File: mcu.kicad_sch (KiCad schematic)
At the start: 32 parts, among them SW2 SW_SPDT, U2 STM32F429ZITx, Y3 Crystal_GND24

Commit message: More MCU wiring
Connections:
- net USB_OTG_FS_ID is gone; now on net UART0_RX: U2.102 (PA10)
- net SPI0_DO: now also U2.43 (PA7); no longer U2.135 (PB5)
- net UART0_RX: no longer U2.137 (PB7)
- net UART1_RX: now also U2.37 (PA3); no longer U2.122 (PD6)
- net UART1_TX: now also U2.36 (PA2); no longer U2.119 (PD5)
- net JTAG0_TDI: now reaches U2.110 (PA15)
- net JTAG0_TDO: now reaches U2.133 (PB3)
- net SPI1_DI: no longer names the net of U2.75 (PB14)
- net SPI1_DO: no longer names the net of U2.76 (PB15)
- net SPI1_SK: no longer names the net of U2.69 (PB10)
- net SWCLK renamed JTAG0_TCK
- net SWDIO renamed JTAG0_TMS
- new net I2C0_SDA: U2.137 (PB7)
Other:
- note added: "1: Boot Flash 3: Boot System Memory (STM Bootloader)"

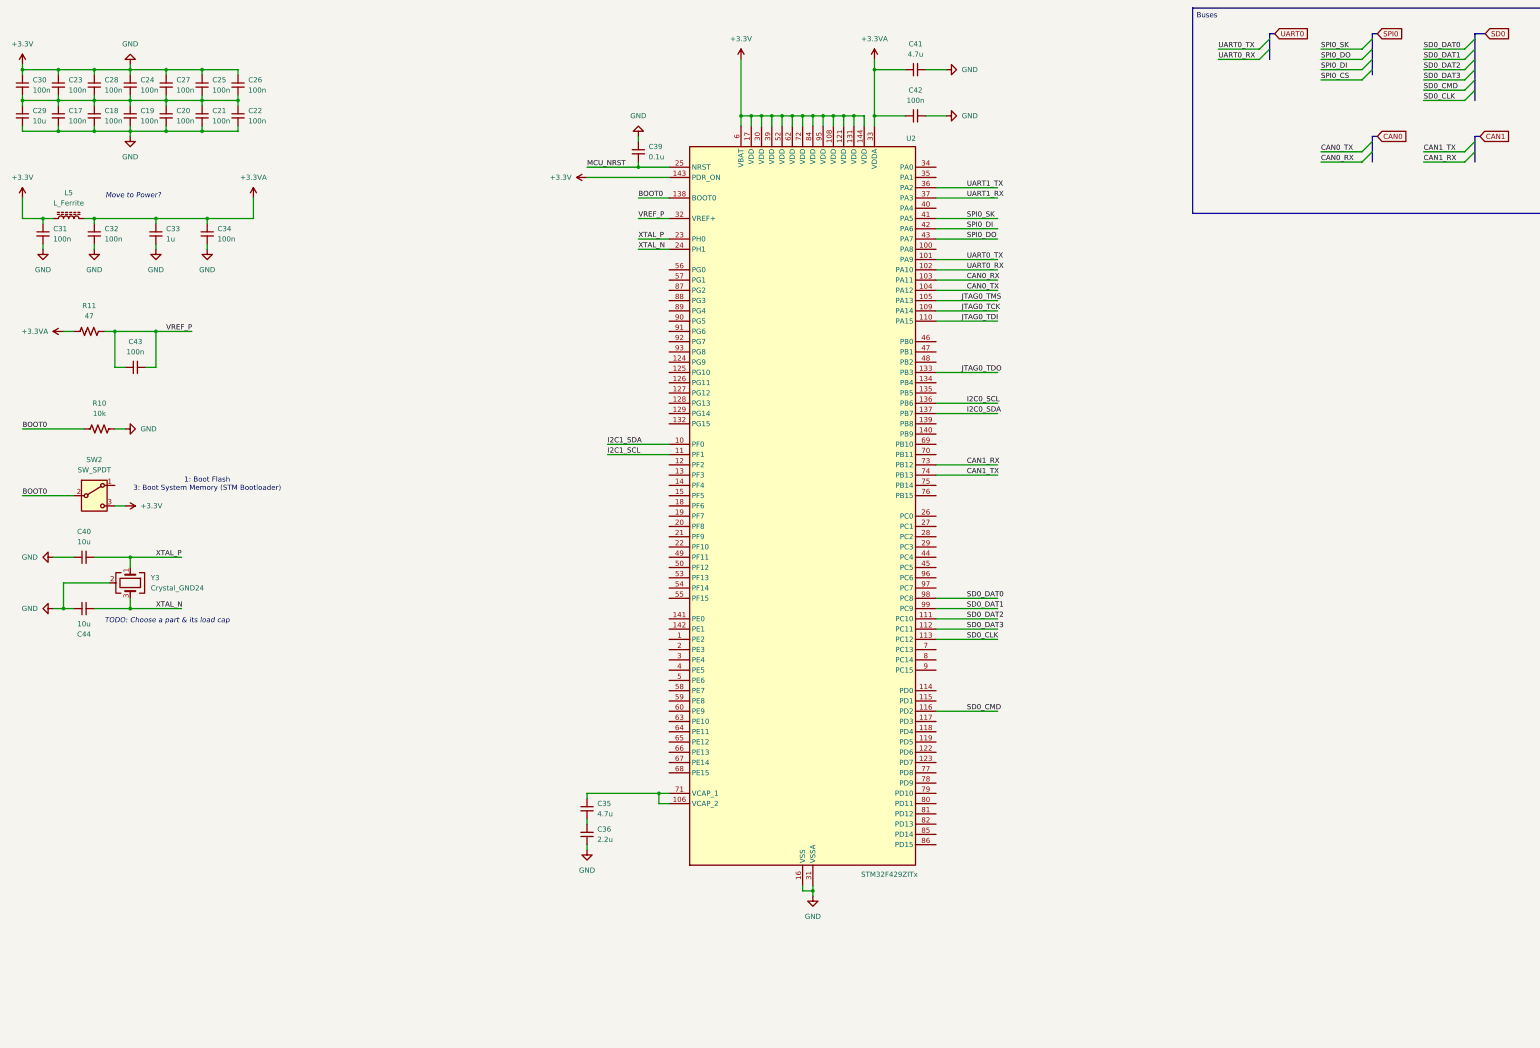
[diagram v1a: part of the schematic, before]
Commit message: A lot re-wiring, added appropriate parts for schematic components. Some re-organization.
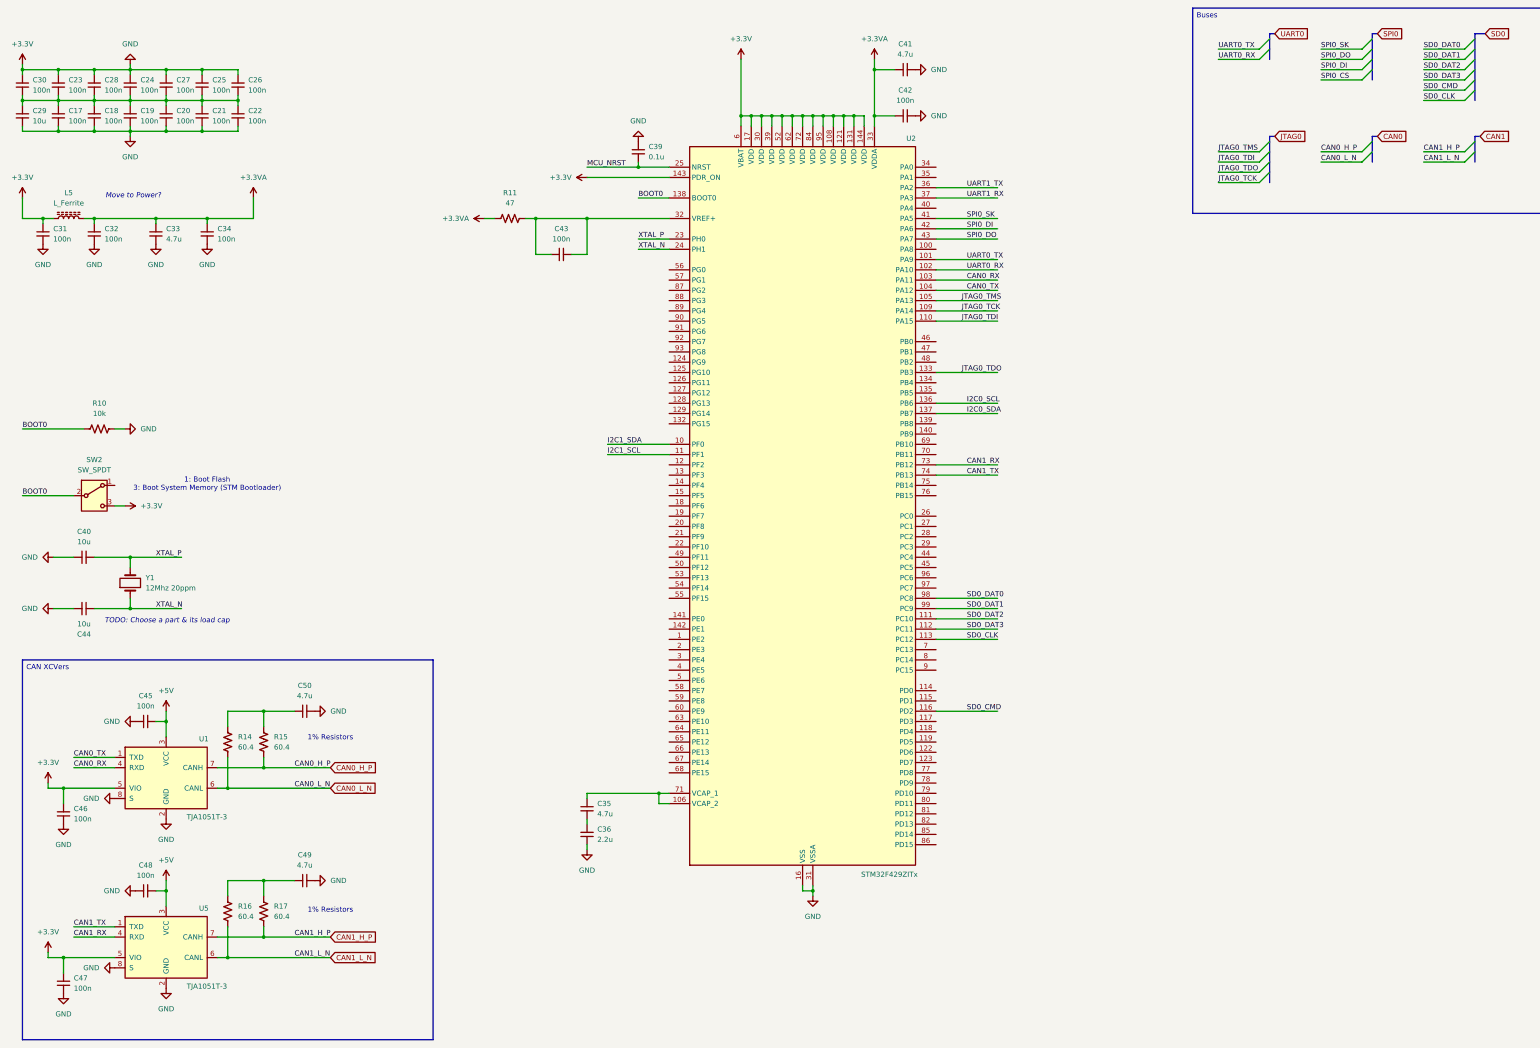
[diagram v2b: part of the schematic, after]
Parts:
- removed Y3: Crystal_GND24, symbol Device:Crystal_GND24
- added C45, C46, C47, C48: 100n, symbol Device:C_Small
- added C49, C50: 4.7u, symbol Device:C_Small
- added R14, R15, R16, R17: 60.4, symbol Device:R_US
- added U1, U5: TJA1051T-3, Package_SO:SOIC-8_3.9x4.9mm_P1.27mm, symbol Interface_CAN_LIN:TJA1051T-3
- added Y1: 12Mhz 20ppm, symbol Device:Crystal
- C33: value 1u -> 4.7u
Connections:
- net +3.3V: now also C45.1, C46.1, C46.2, C47.1, C47.2, C48.1, C49.2, C50.2, U1.2 (GND), U1.5 (VIO), U1.8 (S), U5.2 (GND), U5.5 (VIO), U5.8 (S)
- net CAN0_RX: now also U1.4 (RXD)
- net CAN0_TX: now also U1.1 (TXD)
- net CAN1_RX: now also U5.4 (RXD)
- net CAN1_TX: now also U5.1 (TXD)
- net XTAL_N: now also Y1.1
- net XTAL_P: now also Y1.2
- net VREF_P: no longer names the net of C43.1, C43.2, R11.2, U2.32 (VREF+)
- new net: C49.1, R16.1, R17.1
- new net: C50.1, R14.1, R15.1
- new net +5V: C45.2, C48.2, U1.3 (VCC), U5.3 (VCC)
- new net CAN0_H_P: R15.2, U1.7 (CANH)
- new net CAN0_L_N: R14.2, U1.6 (CANL)
- new net CAN1_H_P: R17.2, U5.7 (CANH)
- new net CAN1_L_N: R16.2, U5.6 (CANL)
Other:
- note added: "1% Resistors"
- moved on the sheet: C41, C42, C43, R11

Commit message: Alot of stuff
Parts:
- removed SW2: SW_SPDT, symbol Switch:SW_SPDT
- added D10: RED_LED1, LED_SMD:LED_0805_2012Metric, symbol Device:LED
- added D6: MCU_GOOD_LED, LED_SMD:LED_0805_2012Metric, symbol Device:LED
- added D7: GREEN_LED1, LED_SMD:LED_0805_2012Metric, symbol Device:LED
- added D9: BLUE_LED1, LED_SMD:LED_0805_2012Metric, symbol Device:LED
- added R20, R22, R23: 3.3k, symbol Device:R_US
- added R25, R26, R28, R29: 560, symbol Device:R_US
- R10: value 10k -> 3.3k
- Y1: footprint (none) -> SamacSys_Parts:ABLS7
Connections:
- net I2C0_SCL is gone; now on net I2C1_SCL: U2.136 (PB6)
- net I2C0_SDA is gone; now on net I2C1_SDA: U2.137 (PB7)
- net UART0_RX is gone; now on net UART1_RX: U2.102 (PA10)
- net UART0_TX is gone; now on net UART1_TX: U2.101 (PA9)
- net +3.3V: now also D10.1 (K), D6.1 (K), D7.1 (K), D9.1 (K), R20.2, R22.2, R23.2
- net CAN0_RX: no longer U2.103 (PA11)
- net CAN0_TX: no longer U2.104 (PA12)
- net CAN1_RX: now also U2.103 (PA11); no longer U2.73 (PB12)
- net CAN1_TX: now also U2.104 (PA12); no longer U2.74 (PB13)
- net I2C1_SCL: now also R20.1; no longer U2.11 (PF1)
- net I2C1_SDA: now also R10.1; no longer U2.10 (PF0)
- net UART1_RX: no longer U2.37 (PA3)
- net UART1_TX: no longer U2.36 (PA2)
- net GPIO8: now reaches U2.124 (PG9)
- net GPIO9: now reaches U2.125 (PG10)
- net GPIO10: now reaches U2.126 (PG11)
- net GPIO11: now reaches U2.127 (PG12)
- net GPIO12: now reaches U2.128 (PG13)
- net GPIO13: now reaches U2.129 (PG14)
- net GPIO14: now reaches U2.132 (PG15)
- net GREEN_LED1: now reaches U2.141 (PE0)
- net GREEN_LED1: now also R26.2
- net BLUE_LED1: now reaches U2.142 (PE1)
- net BLUE_LED1: now also R28.2
- net MCU_BOOT1: now reaches U2.48 (PB2)
- net MCU_GOOD_LED: now reaches U2.56 (PG0)
- net MCU_GOOD_LED: now also R25.2
- net GPIO0: now reaches U2.57 (PG1)
- net RED_LED1: now reaches U2.66 (PE13)
- net RED_LED1: now also R29.2
- net GPIO1: now reaches U2.87 (PG2)
- net GPIO2: now reaches U2.88 (PG3)
- net GPIO3: now reaches U2.89 (PG4)
- net GPIO4: now reaches U2.90 (PG5)
- net GPIO5: now reaches U2.91 (PG6)
- net GPIO6: now reaches U2.92 (PG7)
- net GPIO7: now reaches U2.93 (PG8)
- net BOOT0 renamed MCU_BOOT0
- net MCU_BOOT0: no longer R10.1
- net JTAG0_TCK renamed JTAG_TCK
- net JTAG0_TDI renamed JTAG_TDI
- net JTAG0_TDO renamed JTAG_TDO
- net JTAG0_TMS renamed JTAG_TMS
- net SD0_CLK renamed SD_CLK
- net SD0_CMD renamed SD_CMD
- net SD0_DAT0 renamed SD_DAT0
- net SD0_DAT1 renamed SD_DAT1
- net SD0_DAT2 renamed SD_DAT2
- net SD0_DAT3 renamed SD_DAT3
- net SPI0_DI renamed SPI1_DI
- net SPI0_DO renamed SPI1_DO
- net SPI0_SK renamed SPI1_SK
- new net: D10.2 (A), R29.1
- new net: D6.2 (A), R25.1
- new net: D9.2 (A), R28.1
- new net: D7.2 (A), R26.1
- new net CAN2_RX: U2.73 (PB12)
- new net CAN2_TX: U2.74 (PB13)
- new net I2C2_SCL: R22.1, U2.11 (PF1)
- new net I2C2_SDA: R23.1, U2.10 (PF0)
- new net UART2_RX: U2.37 (PA3)
- new net UART2_TX: U2.36 (PA2)
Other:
- note added: "Use LTST-C170TBKT for all LEDs!"
- note added: "VDDA flitering for ADCs"
- note added: "values for these matter! need fast rise and fall!"
- note removed: "1: Boot Flash 3: Boot System Memory (STM Bootloader)"
- note removed: "Move to Power?"

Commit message: Stuff
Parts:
- C40, C44: value 10u -> 27p
- Y1: value 12Mhz 20ppm -> 12Mhz; footprint SamacSys_Parts:ABLS7 -> SamacSys_Parts:ABLS7M212000MHZD2YT
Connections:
- net SD_DET: now also U2.7 (PC13)
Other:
- note added: "3.3k good value for I2C open-drain"
- note added: "Need 1% Resistors here!"
- note removed: "1% Resistors"
- note removed: "TODO: Choose a part & its load cap"
- note removed: "values for these matter! need fast rise and fall!"
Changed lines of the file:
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@@
 		)
 	)
-	(text "1% Resistors"
+	(text "Need 1% Resistors here!"
 		(exclude_from_sim no)
-		(at 101.6 239.776 0)
+		(at 104.902 239.776 0)
 		(effects
 			(font
@@
 		)
 	)
-	(text "values for these matter! need fast rise and fall!\n"
+	(text "3.3k good value for I2C open-drain"
 		(exclude_from_sim no)
 		(at 160.528 121.666 0)
@@
 		)
 	)
-	(text "values for these matter! need fast rise and fall!\n"
+	(text "3.3k good value for I2C open-drain"
 		(exclude_from_sim no)
 		(at 277.622 110.49 0)
@@
 		)
 	)
-	(text "TODO: Choose a part & its load cap"
+	(text "Need 1% Resistors here!"
 		(exclude_from_sim no)
-		(at 61.214 168.148 0)
-		(effects
-			(font
-				(size 1.27 1.27)
-				(italic yes)
-			)
-		)
-	)
-	(text "1% Resistors"
-		(exclude_from_sim no)
-		(at 101.6 197.104 0)
+		(at 104.902 197.612 0)
 		(effects
 			(font
@@
 	(wire
 		(pts
+			(xy 251.46 175.26) (xy 266.7 175.26)
+		)
+		(stroke
+			(width 0)
+			(type default)
+		)
+	)
+	(wire
+		(pts
 			(xy 223.52 43.18) (xy 223.52 45.72)
 		)
@@
 		)
 	)
+	(label "SD_DET"
+		(at 266.7 175.26 180)
+		(effects
+			(font
+				(size 1.27 1.27)
+			)
+			(justify right bottom)
+		)
+	)
 	(label "GPIO14"
 		(at 374.65 119.38 0)
@@
 			)
 		)
-		(property "Value" "12Mhz 20ppm"
+		(property "Value" "12Mhz"
 			(at 55.88 160.02 90)
 			(show_name no)
@@
 			)
 		)
-		(property "Footprint" "SamacSys_Parts:ABLS7"
+		(property "Footprint" "SamacSys_Parts:ABLS7M212000MHZD2YT"
 			(at 52.07 158.75 0)
 			(hide yes)
@@
 			)
 		)
-		(property "Description" "Two pin crystal"
+		(property "Description" "ABLS7M212000MHZD2YT Two pin crystal 12Mhz 20ppm"
 			(at 52.07 158.75 0)
 			(hide yes)
@@
 			)
 		)
-		(property "Value" "10u"
+		(property "Value" "27p"
 			(at 40.6337 168.91 90)
 			(show_name no)
@@
 			)
 		)
-		(property "Value" "10u"
+		(property "Value" "27p"
 			(at 40.6463 148.59 90)
 			(show_name no)

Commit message: Minor
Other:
- note added: "use nmost for these?"
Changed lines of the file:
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@@
+		)
+	)
+	(text "use nmost for these?"
+		(exclude_from_sim no)
+		(at 370.586 145.288 0)
+		(effects
+			(font
+				(size 1.27 1.27)
+			)
 		)
 	)

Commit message: Stuff
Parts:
- removed D10: RED_LED1, LED_SMD:LED_0805_2012Metric, symbol Device:LED
- added D8: LED3, SamacSys_Parts:LEDC2012X110N, symbol Device:LED
- D6: value MCU_GOOD_LED -> LED1; footprint LED_SMD:LED_0805_2012Metric -> SamacSys_Parts:LEDC2012X110N
- D7: value GREEN_LED1 -> LED2; footprint LED_SMD:LED_0805_2012Metric -> SamacSys_Parts:LEDC2012X110N
- D9: value BLUE_LED1 -> LED4; footprint LED_SMD:LED_0805_2012Metric -> SamacSys_Parts:LEDC2012X110N
- R25, R26, R28, R29: value 560 -> 62
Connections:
- net +3.3V: now also D8.1 (K)
- net GPIO0: now also U2.56 (PG0); no longer U2.57 (PG1)
- net GPIO1: now also U2.57 (PG1); no longer U2.87 (PG2)
- net GPIO10: now also U2.125 (PG10); no longer U2.126 (PG11)
- net GPIO11: now also U2.126 (PG11); no longer U2.127 (PG12)
- net GPIO12: now also U2.127 (PG12); no longer U2.128 (PG13)
- net GPIO13: now also U2.128 (PG13); no longer U2.129 (PG14)
- net GPIO14: now also U2.129 (PG14); no longer U2.132 (PG15)
- net GPIO2: now also U2.87 (PG2); no longer U2.88 (PG3)
- net GPIO3: now also U2.88 (PG3); no longer U2.89 (PG4)
- net GPIO4: now also U2.89 (PG4); no longer U2.90 (PG5)
- net GPIO5: now also U2.90 (PG5); no longer U2.91 (PG6)
- net GPIO6: now also U2.91 (PG6); no longer U2.92 (PG7)
- net GPIO7: now also U2.92 (PG7); no longer U2.93 (PG8)
- net GPIO8: now also U2.93 (PG8); no longer U2.124 (PG9)
- net GPIO9: now also U2.124 (PG9); no longer U2.125 (PG10)
- net at R29.1: now also D9.2 (A)
- net LED3: now reaches U2.1 (PE2)
- net LED3: now also R28.2
- net LED4: now reaches U2.2 (PE3)
- net LED4: now also R29.2
- net at R28.1: now also D8.2 (A); no longer D9.2 (A)
- net BLUE_LED1 renamed LED2
- net LED2: now also R26.2; no longer R28.2
- net GREEN_LED1 renamed LED1
- net LED1: now also R25.2; no longer R26.2
- removed net MCU_GOOD_LED: R25.2, U2.56 (PG0)
- net RED_LED1: no longer names the net of U2.66 (PE13)
- net RED_LED1: no longer R29.2
- new net GPIO15: U2.132 (PG15)
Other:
- note added: "STM32F429 GPIO pins can provide 25mA max We need 15mA for these LEDs"
- note removed: "Use LTST-C170TBKT for all LEDs!"
- note removed: "use nmost for these?"
